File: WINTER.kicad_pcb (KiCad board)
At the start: 6 copper layers, 52 x 34 mm, 106 parts, among them J1 Amphenol ICC 10118193-0001LF, J2 TF-102-15, J3 Screw_Terminal_01x12, J4 Screw_Terminal_01x02, J5 Conn_01x05, J6 Conn_01x04, Q1 SI7232DN-T1-GE3, Q2 SI7232DN-T1-GE3, Q3 SI7232DN-T1-GE3, SW1 A6S-2104-H, U1 LM2940LD-5.0/NOPB, U10 SX1262IMLTRT, U11 MAX-M10S-00B, U12 LM1117LD-3.3/NOPB, U13 74LVC1G04, U2 DRV8210DRLR, U3 MMC5983MA, U4 ICM-42688-P, U5 SKY66105, U6 STM32H725RGV6, U7 MS5607-02BA, U8 ADXL375, U9 74LVC2T45DC, Y1 ECS-2520MV-240-BN, Y2 ATX-11-F-32.000MHZ-F05-T

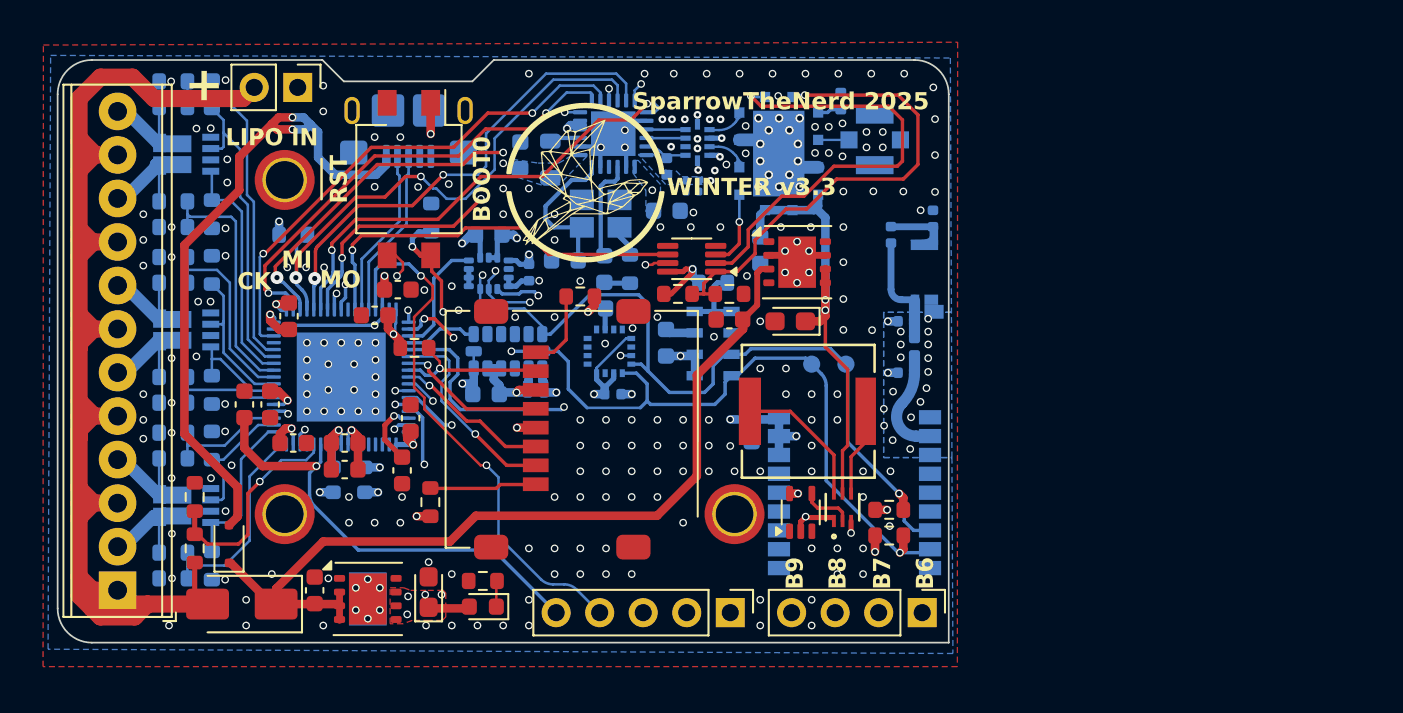
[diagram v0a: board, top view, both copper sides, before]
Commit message: Fix footprints and update rev number
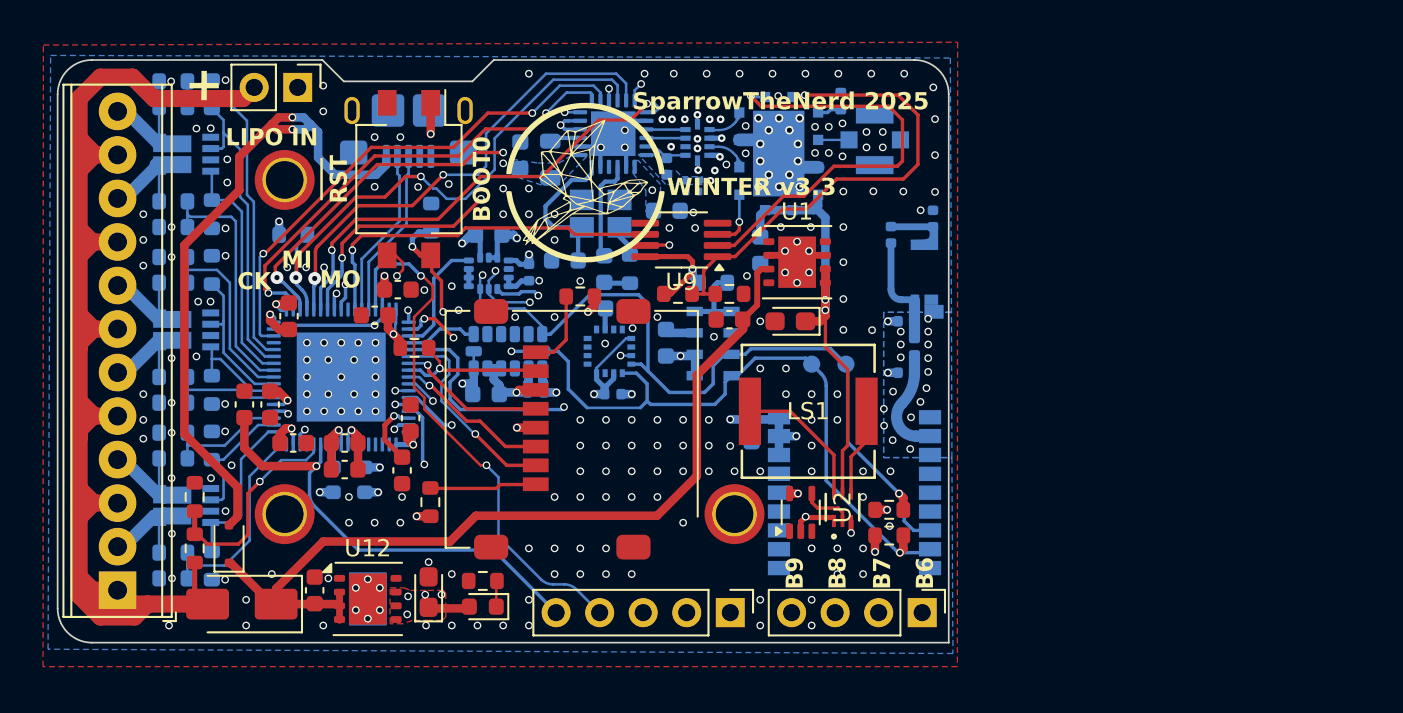
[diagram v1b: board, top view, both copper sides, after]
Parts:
- AE2: footprint rev3footprints:GGBLA.01.A -> WINTERfootprints:GGBLA.01.A
- LS1: footprint rev3footprints:AST0760_MAL -> WINTERfootprints:AST0760_MAL
- Q1, Q2, Q3: footprint rev3footprints:TRANS_SI7232DN-T1-GE3 -> WINTERfootprints:TRANS_SI7232DN-T1-GE3
- U1, U12: footprint Package_SON:WSON-8-1EP_4x4mm_P0.8mm_EP2.2x3mm_ThermalVias -> Package_SON:WSON-8-1EP_4x4mm_P0.8mm_EP2.2x3mm
- U11: footprint rev3footprints:MAX-M10S-00B -> WINTERfootprints:MAX-M10S-00B
- U2: footprint rev3footprints:SOT_210DRLR_TEX -> WINTERfootprints:SOT_210DRLR_TEX
- U3: footprint rev3footprints:MMC5983MA_MEM -> WINTERfootprints:MMC5983MA_MEM
- U4: footprint rev3footprints:PQFN50P300X250X97-14N -> WINTERfootprints:PQFN50P300X250X97-14N
- U5: footprint rev3footprints:SKY66105-11 -> WINTERfootprints:SKY66105-11
- U9: value 74LVC2T45DC -> SN74LVC2T45DC; footprint Package_SO:VSSOP-8_2.3x2mm_P0.5mm -> Package_SO:MSOP-8_3x3mm_P0.65mm
- Y2: footprint rev3footprints:OSC_ATX-11-F-32.000MHZ-F05-T -> WINTERfootprints:OSC_ATX-11-F-32.000MHZ-F05-T
- moved U9 1.25 mm to (174.4, 94.5)
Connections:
- U6 pad 1: +3V3 -> unconnected-(U6-VBAT-Pad1)
- U6 pad 10: Net-(U6-PH0) -> unconnected-(U6-PH0-Pad10)
- U6 pad 12: SWD-NRST -> unconnected-(U6-NRST-Pad12)
- U6 pad 13: LIPO-SENSE -> unconnected-(U6-PC0-Pad13)
- U6 pad 16: +3V3 -> unconnected-(U6-VDDA-Pad16)
- U6 pad 17: SENSE6 -> unconnected-(U6-PA0-Pad17)
- U6 pad 18: PY6 -> unconnected-(U6-PA1-Pad18)
- U6 pad 19: PY5 -> unconnected-(U6-PA2-Pad19)
- U6 pad 20: SENSE5 -> unconnected-(U6-PA3-Pad20)
- U6 pad 22: +3V3 -> unconnected-(U6-VDD-Pad22)
- U6 pad 23: SENSE4 -> unconnected-(U6-PA4-Pad23)
- U6 pad 24: PY4 -> unconnected-(U6-PA5-Pad24)
- U6 pad 25: PY3 -> unconnected-(U6-PA6-Pad25)
- U6 pad 26: SENSE3 -> unconnected-(U6-PA7-Pad26)
- U6 pad 27: SENSE2 -> unconnected-(U6-PC4-Pad27)
- U6 pad 28: PY2 -> unconnected-(U6-PC5-Pad28)
- U6 pad 29: PY1 -> unconnected-(U6-PB0-Pad29)
- U6 pad 30: SENSE1 -> unconnected-(U6-PB1-Pad30)
- U6 pad 32: LoRa_BUSY -> unconnected-(U6-PB10-Pad32)
- U6 pad 33: Net-(C1-Pad1) -> unconnected-(U6-VCAP-Pad33)
- U6 pad 35: +3V3 -> unconnected-(U6-VDD-Pad35)
- U6 pad 36: LoRa_INT -> unconnected-(U6-PB12-Pad36)
- U6 pad 37: SCK_LoRa -> unconnected-(U6-PB13-Pad37)
- U6 pad 38: MISO_LoRa -> unconnected-(U6-PB14-Pad38)
- U6 pad 39: MOSI_LoRa -> unconnected-(U6-PB15-Pad39)
- U6 pad 40: CS_LoRa -> unconnected-(U6-PC6-Pad40)
- U6 pad 41: LoRa_RST -> unconnected-(U6-PC7-Pad41)
- U6 pad 42: SDA -> unconnected-(U6-PC9-Pad42)
- U6 pad 43: SCL -> unconnected-(U6-PA8-Pad43)
- U6 pad 45: LoRa_PA-EN -> unconnected-(U6-PA10-Pad45)
- U6 pad 46: USB_D- -> unconnected-(U6-PA11-Pad46)
- U6 pad 47: USB_D+ -> unconnected-(U6-PA12-Pad47)
- U6 pad 48: SWDIO -> unconnected-(U6-PA13(JTMS-Pad48)
- U6 pad 49: Net-(C1-Pad1) -> unconnected-(U6-VCAP-Pad49)
- U6 pad 51: +3V3 -> unconnected-(U6-VDD-Pad51)
- U6 pad 52: SWCLK -> unconnected-(U6-PA14(JTCK-Pad52)
- U6 pad 53: BUZZ -> unconnected-(U6-PA15(JTDI)-Pad53)
- U6 pad 54: IMU_INT -> unconnected-(U6-PC10-Pad54)
- U6 pad 55: HIGHG_INT -> unconnected-(U6-PC11-Pad55)
- U6 pad 56: MAG_INT -> unconnected-(U6-PC12-Pad56)
- U6 pad 57: CS_SD -> unconnected-(U6-PD2-Pad57)
- U6 pad 58: SCK_SD -> unconnected-(U6-PB3(JTDO-Pad58)
- U6 pad 59: MISO_SD -> unconnected-(U6-PB4(NJTRST)-Pad59)
- U6 pad 60: MOSI_SD -> unconnected-(U6-PB5-Pad60)
- U6 pad 61: SERVO4 -> unconnected-(U6-PB6-Pad61)
- U6 pad 62: SERVO3 -> unconnected-(U6-PB7-Pad62)
- U6 pad 63: /Microcontroller/SWD-BOOT0 -> unconnected-(U6-BOOT0-Pad63)
- U6 pad 64: SERVO2 -> unconnected-(U6-PB8-Pad64)
- U6 pad 65: SERVO1 -> unconnected-(U6-PB9-Pad65)
- U6 pad 66: Net-(C1-Pad1) -> unconnected-(U6-VCAP-Pad66)
- U6 pad 68: +3V3 -> unconnected-(U6-VDD-Pad68)
- U6 pad 7: GNDREF -> unconnected-(U6-VFBSMPS-Pad7)
- U6 pad 9: +3V3 -> unconnected-(U6-VDD-Pad9)
- Y1 pad 3: Net-(U6-PH0) -> unconnected-(Y1-OUT-Pad3)
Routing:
- net +3V3: track 60.1 -> 62.9 mm
- net LoRa_PA-EN: track 23.3 -> 21.5 mm
- net Net-(U6-PH0): track 1.26 -> 0.00 mm
- net (no net): track 0.00 -> 1.26 mm
- net /LoRa Radio/DIO2-2v5: track 26.6 -> 25.5 mm
- net /LoRa Radio/PA-EN-2v5: track 4.50 -> 3.43 mm
- net /LoRa Radio/DIO2: track 23.9 -> 24.9 mm

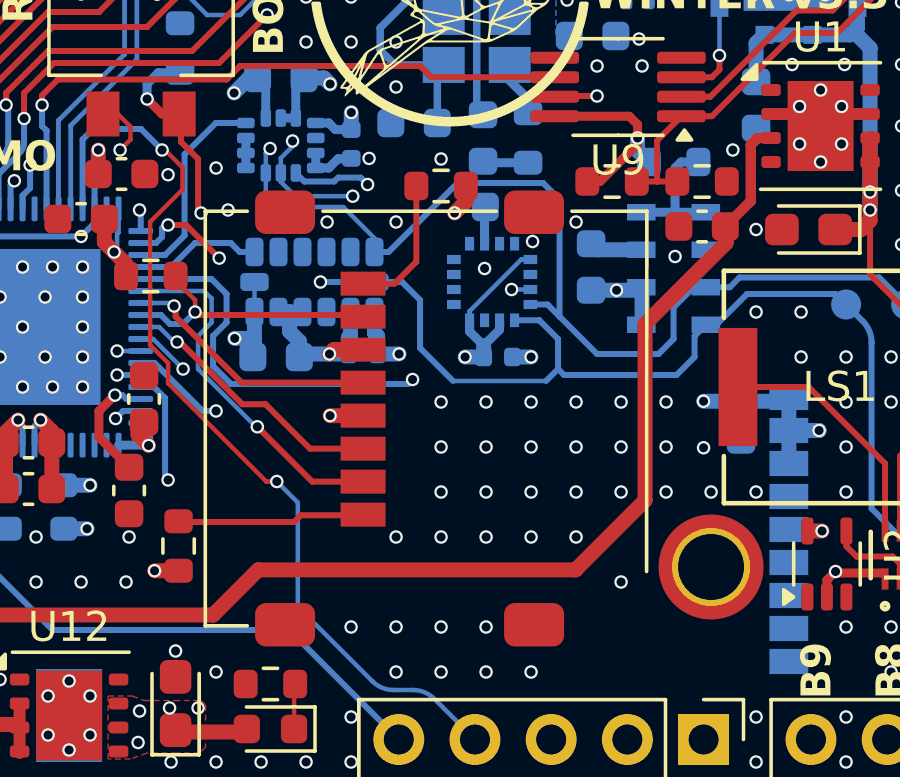
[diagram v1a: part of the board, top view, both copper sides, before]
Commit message: Added previously missing V_CORE 1.35V regulator
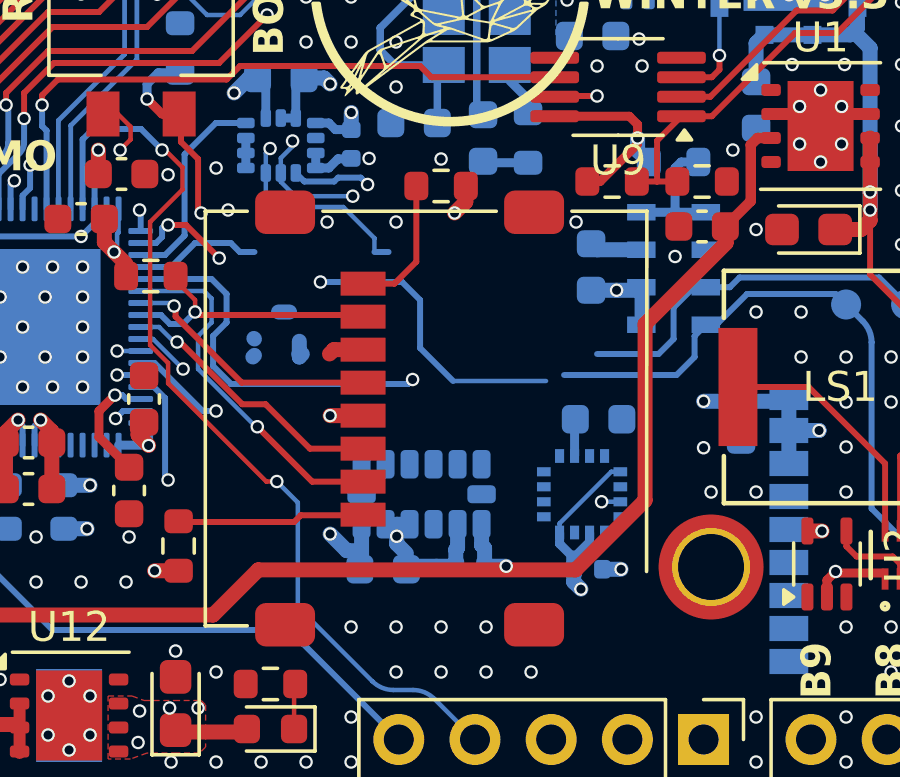
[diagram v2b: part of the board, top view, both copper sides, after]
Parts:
- moved C20 7.92 mm to (166.6, 110.6)
- moved U8 7.92 mm to (167.8, 108.1)
- moved C19 7.92 mm to (169.5, 110.5)
- moved C15 7.68 mm to (173.4, 110.6)
- moved C17 7.68 mm to (173.8, 105.6)
- moved U3 7.68 mm to (173.2, 108.1)
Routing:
- net unconnected-(U6-PC12-Pad56): track 0.00 -> 17.2 mm, vias 0 -> 1
- net MAG_INT: track 17.8 -> 0.62 mm, vias 2 -> 1
- net SDA: track 56.6 -> 42.9 mm
- net unconnected-(U6-PC11-Pad55): track 0.00 -> 4.25 mm
- net HIGHG_INT: track 4.25 -> 0.00 mm
- net SCL: track 60.3 -> 56.8 mm
- net +3V3: track 62.9 -> 63.7 mm
- net GNDREF: vias 265 -> 239

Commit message: Some layout tweaks
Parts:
- added U15: TPS7A20xxxDQN, Package_SON:Texas_X2SON-4_1x1mm_P0.65mm, F.Cu at (150.9, 101.7)
- moved R22 13.5 mm to (164.0, 102.7), turned to -90 degrees
- moved C16 12.0 mm to (173.5, 100.4)
- moved C18 12.0 mm to (175.8, 102.6)
- moved U4 12.0 mm to (173.5, 102.7)
- moved U7 8.96 mm to (167.5, 102.7), turned to 90 degrees
- moved C21 7.76 mm to (167.5, 105.4), turned to 0 degrees
- moved Y2 0.94 mm to (169.8, 93.9)
- moved C28 0.94 mm to (167.7, 96.6)
- moved C27 0.94 mm to (170.0, 97.1)
- moved R26 0.94 mm to (171.5, 97.1)
- moved C4 0.25 mm to (151.6, 98.7)
- moved J4 0.12 mm to (152.1, 85.6)
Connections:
- C1 pad 1: Net-(C1-Pad1) -> +1V35
- C3 pad 1: Net-(C1-Pad1) -> +1V35
- U6 pad 1: unconnected-(U6-VBAT-Pad1) -> +3V3
- U6 pad 10: unconnected-(U6-PH0-Pad10) -> Net-(U6-PH0)
- U6 pad 12: unconnected-(U6-NRST-Pad12) -> SWD-NRST
- U6 pad 13: unconnected-(U6-PC0-Pad13) -> LIPO-SENSE
- U6 pad 16: unconnected-(U6-VDDA-Pad16) -> +3V3
- U6 pad 17: unconnected-(U6-PA0-Pad17) -> SENSE6
- U6 pad 18: unconnected-(U6-PA1-Pad18) -> PY6
- U6 pad 19: unconnected-(U6-PA2-Pad19) -> PY5
- U6 pad 20: unconnected-(U6-PA3-Pad20) -> SENSE5
- U6 pad 22: unconnected-(U6-VDD-Pad22) -> +3V3
- U6 pad 23: unconnected-(U6-PA4-Pad23) -> SENSE4
- U6 pad 24: unconnected-(U6-PA5-Pad24) -> PY4
- U6 pad 25: unconnected-(U6-PA6-Pad25) -> PY3
- U6 pad 26: unconnected-(U6-PA7-Pad26) -> SENSE3
- U6 pad 27: unconnected-(U6-PC4-Pad27) -> SENSE2
- U6 pad 28: unconnected-(U6-PC5-Pad28) -> PY2
- U6 pad 29: unconnected-(U6-PB0-Pad29) -> PY1
- U6 pad 30: unconnected-(U6-PB1-Pad30) -> SENSE1
- U6 pad 32: unconnected-(U6-PB10-Pad32) -> LoRa_BUSY
- U6 pad 33: unconnected-(U6-VCAP-Pad33) -> +1V35
- U6 pad 35: unconnected-(U6-VDD-Pad35) -> +3V3
- U6 pad 36: unconnected-(U6-PB12-Pad36) -> LoRa_INT
- U6 pad 37: unconnected-(U6-PB13-Pad37) -> SCK_LoRa
- U6 pad 38: unconnected-(U6-PB14-Pad38) -> MISO_LoRa
- U6 pad 39: unconnected-(U6-PB15-Pad39) -> MOSI_LoRa
- U6 pad 40: unconnected-(U6-PC6-Pad40) -> CS_LoRa
- U6 pad 41: unconnected-(U6-PC7-Pad41) -> LoRa_RST
- U6 pad 42: unconnected-(U6-PC9-Pad42) -> SDA
- U6 pad 43: unconnected-(U6-PA8-Pad43) -> SCL
- U6 pad 45: unconnected-(U6-PA10-Pad45) -> LoRa_PA-EN
- U6 pad 46: unconnected-(U6-PA11-Pad46) -> USB_D-
- U6 pad 47: unconnected-(U6-PA12-Pad47) -> USB_D+
- U6 pad 48: unconnected-(U6-PA13(JTMS-Pad48) -> SWDIO
- U6 pad 49: unconnected-(U6-VCAP-Pad49) -> +1V35
- U6 pad 51: unconnected-(U6-VDD-Pad51) -> +3V3
- U6 pad 52: unconnected-(U6-PA14(JTCK-Pad52) -> SWCLK
- U6 pad 53: unconnected-(U6-PA15(JTDI)-Pad53) -> BUZZ
- U6 pad 54: unconnected-(U6-PC10-Pad54) -> IMU_INT
- U6 pad 55: unconnected-(U6-PC11-Pad55) -> HIGHG_INT
- U6 pad 56: unconnected-(U6-PC12-Pad56) -> MAG_INT
- U6 pad 57: unconnected-(U6-PD2-Pad57) -> CS_SD
- U6 pad 58: unconnected-(U6-PB3(JTDO-Pad58) -> SCK_SD
- U6 pad 59: unconnected-(U6-PB4(NJTRST)-Pad59) -> MISO_SD
- U6 pad 60: unconnected-(U6-PB5-Pad60) -> MOSI_SD
- U6 pad 61: unconnected-(U6-PB6-Pad61) -> SERVO4
- U6 pad 62: unconnected-(U6-PB7-Pad62) -> SERVO3
- U6 pad 63: unconnected-(U6-BOOT0-Pad63) -> /Microcontroller/SWD-BOOT0
- U6 pad 64: unconnected-(U6-PB8-Pad64) -> SERVO2
- U6 pad 65: unconnected-(U6-PB9-Pad65) -> SERVO1
- U6 pad 66: unconnected-(U6-VCAP-Pad66) -> +1V35
- U6 pad 68: unconnected-(U6-VDD-Pad68) -> +3V3
- U6 pad 7: unconnected-(U6-VFBSMPS-Pad7) -> GNDREF
- U6 pad 9: unconnected-(U6-VDD-Pad9) -> +3V3
- Y1 pad 3: unconnected-(Y1-OUT-Pad3) -> Net-(U6-PH0)
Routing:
- net +1V35: track 0.00 -> 28.0 mm, vias 0 -> 3
- net MAG_INT: track 0.62 -> 22.3 mm, vias 1 -> 2
- net Net-(C1-Pad1): track 19.7 -> 0.00 mm, vias 3 -> 0
- net SDA: track 42.9 -> 62.1 mm, vias 3 -> 8
- net unconnected-(U6-PC12-Pad56): track 17.2 -> 0.00 mm, vias 1 -> 0
- net SCL: track 56.8 -> 73.0 mm
- net HIGHG_INT: track 0.00 -> 13.8 mm
- net IMU_INT: track 6.91 -> 19.9 mm
- net unconnected-(U6-PC11-Pad55): track 4.25 -> 0.00 mm
- net +3V3: track 63.7 -> 67.1 mm, vias 38 -> 39
- net Net-(U6-PH0): track 0.00 -> 1.26 mm
- net (no net): track 1.26 -> 0.00 mm
- net SCK_LoRa: track 32.6 -> 33.8 mm
- net GNDREF: track 38.1 -> 37.0 mm, vias 239 -> 254
- net /LoRa Radio/TCXO-Comp: track 9.05 -> 10.0 mm
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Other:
- board text added: "SWC"
- board text added: "SWD"
- board text added: "WINTER v4"
- board text removed: "SWCLK"
- board text removed: "SWDIO"
- board text removed: "WINTER v3.3"
